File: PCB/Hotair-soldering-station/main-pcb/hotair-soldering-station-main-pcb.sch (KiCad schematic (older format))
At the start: 31 parts, among them J1 fan_reg_pot, J2 main-board-conn

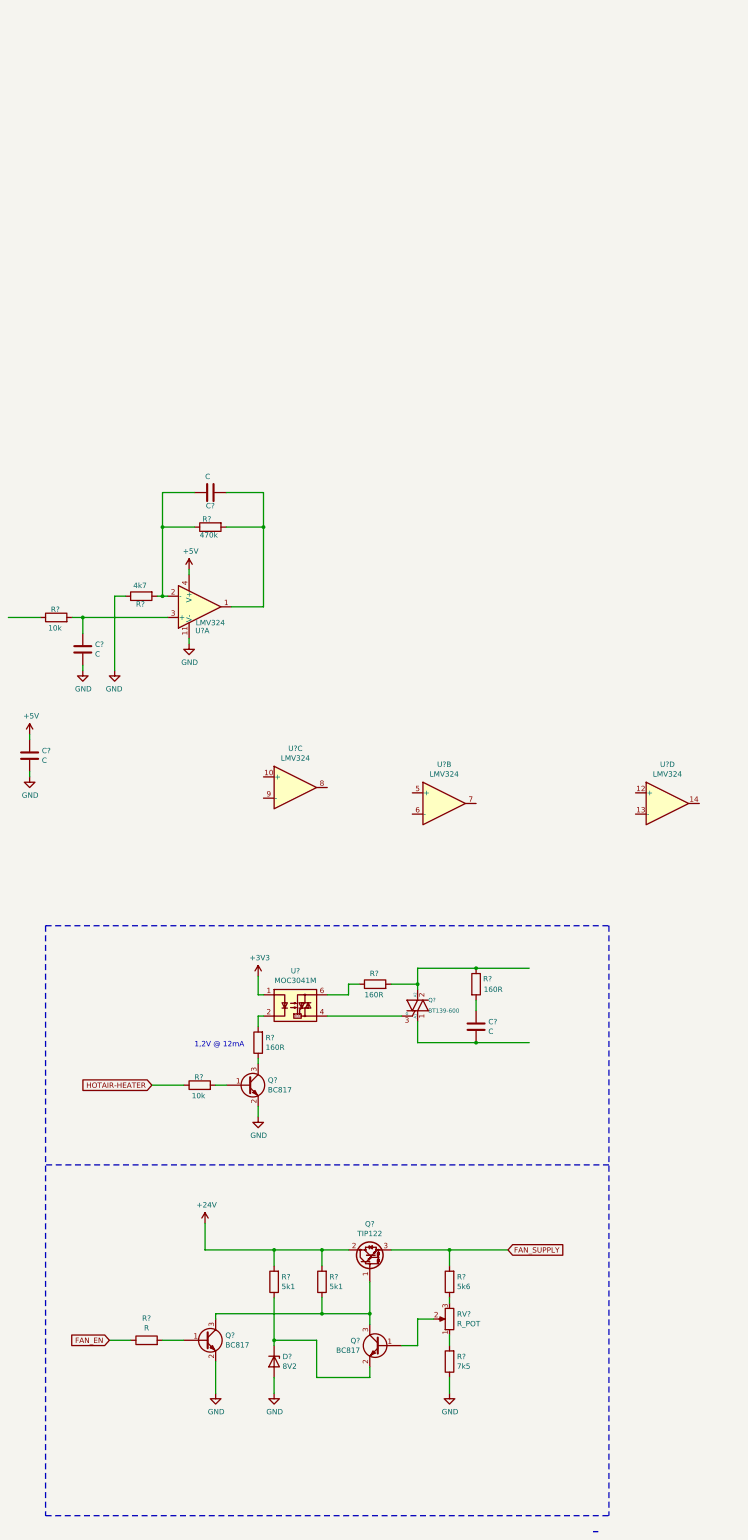
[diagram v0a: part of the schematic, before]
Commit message: schematic update
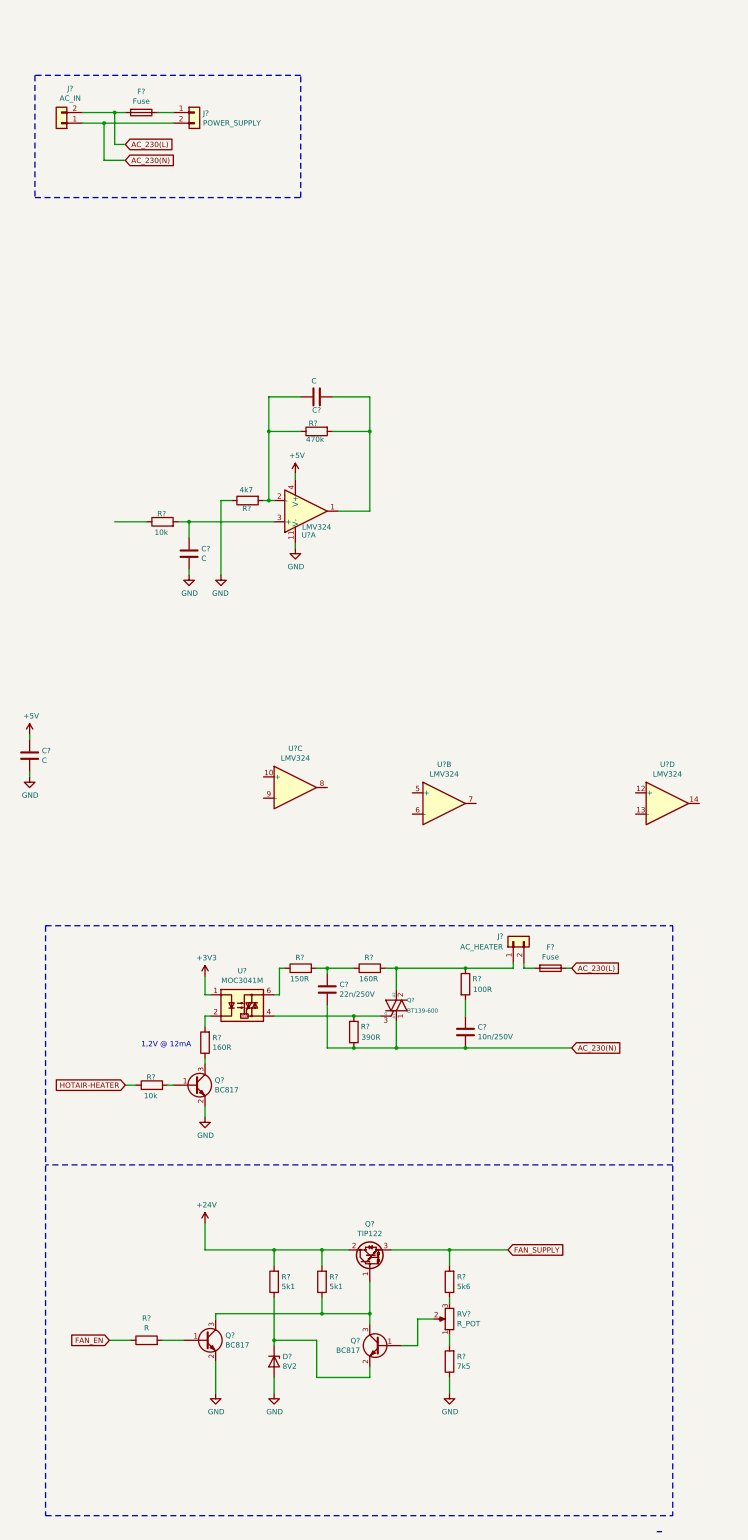
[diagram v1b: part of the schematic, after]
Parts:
- added C?: 22n/250V, symbol Device:C
- added F? (x2): Fuse, symbol Device:Fuse
- added J?: AC_HEATER, symbol Connector_Generic:Conn_01x02
- added J?: AC_IN, symbol Connector_Generic:Conn_01x02
- added J?: POWER_SUPPLY, symbol Connector_Generic:Conn_01x02
- added R?: 390R, Capacitors:0805, symbol Device:R
- added R?: 150R, Capacitors:0805, symbol Device:R
- C?: value C -> 10n/250V
- R?: value 160R -> 100R
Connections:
- net labels added: AC_230(L), AC_230(N)
- wire segments 90 -> 109
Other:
- moved on the sheet: C?, Q?, R?, U?, U?A

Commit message: add heater controll circuit, add sch block structure
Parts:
- added C?: 680u/35V, symbol Device:CP
- added D?: D_Zener, symbol Device:D_Zener
- added F?: Fuse, symbol Device:Fuse
- added J?: 24V_IN, symbol Connector_Generic:Conn_01x02
- added J?: Conn_01x05, symbol Connector_Generic:Conn_01x05
- added Q?: FP3055LP, Package_TO_SOT_THT:TO-220-3_Vertical, symbol Device:Q_NMOS_GDS
- added Q?: BC817, Package_TO_SOT_SMD:SOT-23, symbol Transistor_BJT:BC817
- added R?: 4k7, Capacitors:0805, symbol Device:R
- added R?: 1k, Capacitors:0805, symbol Device:R
- added R?: 100R, Capacitors:0805, symbol Device:R
- added R?: 4,7k, Capacitors:0805, symbol Device:R
- added R?: 10k, Capacitors:0805, symbol Device:R
- added U?: AMS1117-3.3, Package_TO_SOT_SMD:SOT-223-3_TabPin2, symbol Regulator_Linear:AMS1117-3.3
- C?: value C -> 100n
- R?: value 10k -> 1k
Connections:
- net +24V: now also C?.1, F?.1, J?.1 (Pin_1)
- net +5V: now also R?.1
- net GND: now also C?.2, D?.2 (A), J?.1 (Pin_1), J?.4 (Pin_4), J?.5 (Pin_5), Q?.2 (E), Q?.3 (S), R?.1, U?.1 (GND)
- net at C?.1, R?.2, U?.1: now also R?.1
- net SOLDERING_IRON_THERM: now reaches R?.1
- net SOLDERING_IRON_THERM: now also J?.3 (Pin_3)
- net HOTAIR-HEATER renamed HOTAIR_HEATER_CTRL
- new net: F?.2, J?.2 (Pin_2)
- new net: Q?.1 (G), R?.1
- new net: Q?.1 (B), R?.1, R?.2
- new net: Q?.3 (C), R?.2, R?.2
- new net SOLDERING_IRON_HEATER: J?.2 (Pin_2), Q?.2 (D)
- new net SOLD_IRON_HEATER_CTRL: R?.2
- new net THERM_IRON_ADC: D?.1 (K), R?.2
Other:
- note added: "Front PCB connector"
- note added: "HOT-AIR"
- note added: "Heater controll"
- note added: "SMD Rework, Soldering iron - Main PCB"
- note added: "Soldering iron"
- note added: "Soldering iron connector\n"
- note added: "Thermocouple amplifier"
- note removed: "SMD Rework, Soldering station - Front PCB"
- moved on the sheet: C?, D?, F?, J1, J2, J?, Q?, R?, RV?, U?, U?A, U?B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

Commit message: schematic update
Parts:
- added C?: 100n, symbol Device:C
- added C?: C, symbol Device:C
- added D?: D_Zener, symbol Device:D_Zener
- added J?: Conn_01x06, symbol Connector_Generic:Conn_01x06
- added J?: Conn_01x05, symbol Connector_Generic:Conn_01x05
- added R?: 470k, Capacitors:0805, symbol Device:R
- added R? (x2): 4k7, Capacitors:0805, symbol Device:R
- added R?: 1k, Capacitors:0805, symbol Device:R
- added U?: STM32F030K6Tx, Package_QFP:LQFP-32_7x7mm_P0.8mm, symbol MCU_ST_STM32F0:STM32F030K6Tx
- C?: value C -> 100n
- C?: value C -> 8,2n
- D?: value D_Zener -> 3v6
- R?: value 4k7 -> 510R
- R?: value 1k -> 39k
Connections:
- net +3V3: now also J?.2 (Pin_2), U?.1 (VDD), U?.17 (VDD), U?.5 (VDDA)
- net 7SEG_CLK: now also U?.11 (PA5)
- net 7SEG_DIN: now also U?.13 (PA7)
- net 7SEG_LATCH: now also U?.12 (PA6)
- net FAN_SUPPLY: now also J?.1 (Pin_1)
- net GND: now also C?.2, D?.2 (A), J?.3 (Pin_3), J?.4 (Pin_4), J?.5 (Pin_5), R?.1, U?.16 (VSS), U?.32 (VSS)
- net HOTAIR_DOWN_SW: now also U?.28 (PB5)
- net HOTAIR_HEATER_CTRL: now also U?.10 (PA4)
- net HOTAIR_ON_SW: now also U?.15 (PB1)
- net HOTAIR_UP_SW: now also U?.29 (PB6)
- net SOLDERING_IRON_THERM: now also J?.3 (Pin_3)
- net SOLDER_DOWN_SW: now also U?.26 (PB3)
- net SOLDER_ON_SW: now also U?.14 (PB0)
- net SOLDER_UP_SW: now also U?.27 (PB4)
- net SOLD_IRON_HEATER_CTRL: now also U?.9 (PA3)
- net THERM_IRON_ADC: now also U?.6 (PA0)
- net at U?.5 (+): now also C?.2, R?.1, R?.2
- net at U?.6 (-): now also C?.1, R?.2
- net at U?.7: now also C?.1, R?.1, R?.2
- new net BUZZER: U?.18 (PA8)
- new net HOTAIR_REED_SW: J?.2 (Pin_2), U?.30 (PB7)
- new net HOTAIR_THERM: R?.1
- new net RST: J?.1 (Pin_1), U?.4 (NRST)
- new net SWCLK: J?.5 (Pin_5), U?.24 (PA14)
- new net SWDIO: J?.4 (Pin_4), U?.23 (PA13)
- new net THERM_HOTAIR_ADC: D?.1 (K), R?.2, U?.7 (PA1)
- new net UART_DBG_TX: J?.6 (Pin_6), U?.8 (PA2)
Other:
- note added: "HOTAIR connector\n"
- moved on the sheet: C?, D?, F?, J1, J2, J?, Q?, R?, RV?, U?, U?B, U?C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

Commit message: schematic update
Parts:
- added R? (x2): 0R, Capacitors:0805, symbol Device:R
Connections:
- net GND: now also R?.1, R?.1; no longer J?.4 (Pin_4), J?.4 (Pin_4)
- new net: J?.4 (Pin_4), R?.2 (x2)
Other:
- note added: "Microcontroller"
- moved on the sheet: J?, U?
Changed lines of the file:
@@
 L Connector_Generic:Conn_01x05 J?
 U 1 1 5F810B18
-P 9525 11900
-F 0 "J?" H 9605 11942 50  0000 L CNN
-F 1 "Conn_01x05" H 9605 11851 50  0000 L CNN
-F 2 "" H 9525 11900 50  0001 C CNN
-F 3 "~" H 9525 11900 50  0001 C CNN
-	1    9525 11900
+P 9550 11900
+F 0 "J?" H 9630 11942 50  0000 L CNN
+F 1 "Conn_01x05" H 9630 11851 50  0000 L CNN
+F 2 "" H 9550 11900 50  0001 C CNN
+F 3 "~" H 9550 11900 50  0001 C CNN
+	1    9550 11900
 	1    0    0    -1
 $EndComp
@@
 L power:GND #PWR?
 U 1 1 5F812675
-P 9225 12150
-F 0 "#PWR?" H 9225 11900 50  0001 C CNN
-F 1 "GND" H 9230 11977 50  0000 C CNN
-F 2 "" H 9225 12150 50  0001 C CNN
-F 3 "" H 9225 12150 50  0001 C CNN
-	1    9225 12150
-	1    0    0    -1
-$EndComp
-Wire Wire Line
-	9175 11900 9325 11900
-Wire Wire Line
-	9325 11800 9175 11800
-Text GLabel 9175 11800 0    50   Input ~ 0
+P 9250 12150
+F 0 "#PWR?" H 9250 11900 50  0001 C CNN
+F 1 "GND" H 9255 11977 50  0000 C CNN
+F 2 "" H 9250 12150 50  0001 C CNN
+F 3 "" H 9250 12150 50  0001 C CNN
+	1    9250 12150
+	1    0    0    -1
+$EndComp
+Wire Wire Line
+	9200 11900 9350 11900
+Wire Wire Line
+	9350 11800 9200 11800
+Text GLabel 9200 11800 0    50   Input ~ 0
 SOLDERING_IRON_HEATER
-Text GLabel 9175 11900 0    50   Input ~ 0
+Text GLabel 9200 11900 0    50   Input ~ 0
 SOLDERING_IRON_THERM
 Text GLabel 10275 6575 2    50   Input ~ 0
@@
 L power:+24V #PWR?
 U 1 1 5F850C84
-P 9075 11500
-F 0 "#PWR?" H 9075 11350 50  0001 C CNN
-F 1 "+24V" H 9090 11673 50  0000 C CNN
-F 2 "" H 9075 11500 50  0001 C CNN
-F 3 "" H 9075 11500 50  0001 C CNN
-	1    9075 11500
-	1    0    0    -1
-$EndComp
-Wire Wire Line
-	9075 11700 9075 11500
-Wire Wire Line
-	9075 11700 9325 11700
-Wire Wire Line
-	9225 12000 9325 12000
-Wire Wire Line
-	9225 12000 9225 12100
+P 9100 11500
+F 0 "#PWR?" H 9100 11350 50  0001 C CNN
+F 1 "+24V" H 9115 11673 50  0000 C CNN
+F 2 "" H 9100 11500 50  0001 C CNN
+F 3 "" H 9100 11500 50  0001 C CNN
+	1    9100 11500
+	1    0    0    -1
+$EndComp
+Wire Wire Line
+	9100 11700 9100 11500
+Wire Wire Line
+	9100 11700 9350 11700
 $Comp
 L power:+24V #PWR?
@@
 L Regulator_Linear:AMS1117-3.3 U?
 U 1 1 5F87AB31
-P 5375 2450
-F 0 "U?" H 5375 2692 50  0000 C CNN
-F 1 "AMS1117-3.3" H 5375 2601 50  0000 C CNN
-F 2 "Package_TO_SOT_SMD:SOT-223-3_TabPin2" H 5375 2650 50  0001 C CNN
-F 3 "http://www.advanced-monolithic.com/pdf/ds1117.pdf" H 5475 2200 50  0001 C CNN
-	1    5375 2450
+P 6025 2350
+F 0 "U?" H 6025 2592 50  0000 C CNN
+F 1 "AMS1117-3.3" H 6025 2501 50  0000 C CNN
+F 2 "Package_TO_SOT_SMD:SOT-223-3_TabPin2" H 6025 2550 50  0001 C CNN
+F 3 "http://www.advanced-monolithic.com/pdf/ds1117.pdf" H 6125 2100 50  0001 C CNN
+	1    6025 2350
 	1    0    0    -1
 $EndComp
@@
 L power:GND #PWR?
 U 1 1 5F9705C8
-P 5375 2800
-F 0 "#PWR?" H 5375 2550 50  0001 C CNN
-F 1 "GND" H 5380 2627 50  0000 C CNN
-F 2 "" H 5375 2800 50  0001 C CNN
-F 3 "" H 5375 2800 50  0001 C CNN
-	1    5375 2800
-	1    0    0    -1
-$EndComp
-Wire Wire Line
-	5375 2800 5375 2750
+P 6025 2700
+F 0 "#PWR?" H 6025 2450 50  0001 C CNN
+F 1 "GND" H 6030 2527 50  0000 C CNN
+F 2 "" H 6025 2700 50  0001 C CNN
+F 3 "" H 6025 2700 50  0001 C CNN
+	1    6025 2700
+	1    0    0    -1
+$EndComp
+Wire Wire Line
+	6025 2700 6025 2650
 $Comp
 L Device:R R?
@@
 SOLDERING_IRON_THERM
 Wire Wire Line
-	9325 12100 9225 12100
-Connection ~ 9225 12100
-Wire Wire Line
-	9225 12100 9225 12150
+	9350 12100 9250 12100
+Wire Wire Line
+	9250 12100 9250 12150
 Wire Notes Line
 	7325 10875 11775 10875
@@
 	4425 11825 4725 11825
 Connection ~ 4425 11825
-Text GLabel 2100 11925 0    50   Input ~ 0
-HOTAIR_THERM
 Text GLabel 4725 11825 2    50   Input ~ 0
 THERM_HOTAIR_ADC
@@
 L Connector_Generic:Conn_01x05 J?
 U 1 1 5FAE215C
-P 2925 13900
-F 0 "J?" H 3005 13942 50  0000 L CNN
-F 1 "Conn_01x05" H 3005 13851 50  0000 L CNN
-F 2 "" H 2925 13900 50  0001 C CNN
-F 3 "~" H 2925 13900 50  0001 C CNN
-	1    2925 13900
+P 2900 13900
+F 0 "J?" H 2980 13942 50  0000 L CNN
+F 1 "Conn_01x05" H 2980 13851 50  0000 L CNN
+F 2 "" H 2900 13900 50  0001 C CNN
+F 3 "~" H 2900 13900 50  0001 C CNN
+	1    2900 13900
 	1    0    0    -1
 $EndComp
@@
 L power:GND #PWR?
 U 1 1 5FAE2162
-P 2625 14150
-F 0 "#PWR?" H 2625 13900 50  0001 C CNN
-F 1 "GND" H 2630 13977 50  0000 C CNN
-F 2 "" H 2625 14150 50  0001 C CNN
-F 3 "" H 2625 14150 50  0001 C CNN
-	1    2625 14150
-	1    0    0    -1
-$EndComp
-Wire Wire Line
-	2575 13900 2725 13900
-Wire Wire Line
-	2725 13800 2575 13800
-Text GLabel 2575 13900 0    50   Input ~ 0
+P 2600 14150
+F 0 "#PWR?" H 2600 13900 50  0001 C CNN
+F 1 "GND" H 2605 13977 50  0000 C CNN
+F 2 "" H 2600 14150 50  0001 C CNN
+F 3 "" H 2600 14150 50  0001 C CNN
+	1    2600 14150
+	1    0    0    -1
+$EndComp
+Wire Wire Line
+	2550 13900 2700 13900
+Wire Wire Line
+	2700 13800 2550 13800
+Text GLabel 2550 13900 0    50   Input ~ 0
 SOLDERING_IRON_THERM
-Wire Wire Line
-	2625 14000 2725 14000
-Wire Wire Line
-	2625 14000 2625 14100
-Wire Wire Line
-	2725 14100 2625 14100
-Connection ~ 2625 14100
-Wire Wire Line
-	2625 14100 2625 14150
 Text Notes 775  13075 0    98   ~ 0
 HOTAIR connector\n
@@
 Wire Notes Line
 	650  4925 650  14675
-Text GLabel 2575 13800 0    50   Input ~ 0
+Text GLabel 2550 13800 0    50   Input ~ 0
 HOTAIR_REED_SW
-Text GLabel 2575 13700 0    50   Input ~ 0
+Text GLabel 2550 13700 0    50   Input ~ 0
 FAN_SUPPLY
 Wire Wire Line
-	2575 13700 2725 13700
+	2550 13700 2700 13700
 Wire Notes Line
 	6950 5550 12675 5550
+Text Notes 12950 5450 0    236  ~ 47
+Microcontroller
+Text GLabel 2100 11925 0    50   Input ~ 0
+HOTAIR_THERM
+$Comp
+L Device:R R?
+U 1 1 5F8115BA
+P 2450 14000
+F 0 "R?" V 2275 14050 50  0000 R CNN
+F 1 "0R" V 2350 14050 50  0000 R CNN
+F 2 "Capacitors:0805" V 2380 14000 50  0001 C CNN
+F 3 "~" H 2450 14000 50  0001 C CNN
+	1    2450 14000
+	0    -1   -1   0
+$EndComp
+Wire Wire Line
+	2700 14100 2600 14100
+Wire Wire Line
+	2600 14100 2600 14150
+Wire Wire Line
+	2700 14000 2600 14000
+$Comp
+L power:GND #PWR?
+U 1 1 5F839D58
+P 2300 14150
+F 0 "#PWR?" H 2300 13900 50  0001 C CNN
+F 1 "GND" H 2305 13977 50  0000 C CNN
+F 2 "" H 2300 14150 50  0001 C CNN
+F 3 "" H 2300 14150 50  0001 C CNN
+	1    2300 14150
+	1    0    0    -1
+$EndComp
+Wire Wire Line
+	2300 14150 2300 14000
+$Comp
+L Device:R R?
+U 1 1 5F8479CC
+P 9100 12000
+F 0 "R?" V 9000 12050 50  0000 R CNN
+F 1 "0R" V 8925 12050 50  0000 R CNN
+F 2 "Capacitors:0805" V 9030 12000 50  0001 C CNN
+F 3 "~" H 9100 12000 50  0001 C CNN
+	1    9100 12000
+	0    -1   -1   0
+$EndComp
+Wire Wire Line
+	9350 12000 9250 12000
+$Comp
+L power:GND #PWR?
+U 1 1 5F864043
+P 8900 12150
+F 0 "#PWR?" H 8900 11900 50  0001 C CNN
+F 1 "GND" H 8905 11977 50  0000 C CNN
+F 2 "" H 8900 12150 50  0001 C CNN
+F 3 "" H 8900 12150 50  0001 C CNN
+	1    8900 12150
+	1    0    0    -1
+$EndComp
+Wire Wire Line
+	8900 12150 8900 12000
+Wire Wire Line
+	8900 12000 8950 12000
 $EndSCHEMATC

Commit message: main schematic update, front pcb routing
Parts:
- added C? (x3): 100n, symbol Device:C
- added C?: 47u, symbol Device:CP
- added C?: 10u, symbol Device:CP
- added MOD?: LM2596-Step-Down, symbol My-Lib:LM2596-Step-Down
- added R?: 0R, Capacitors:0805, symbol Device:R
- added R?: 4k7, Capacitors:0805, symbol Device:R
- added R? (x4): 10k, Capacitors:0805, symbol Device:R
- added U?: DS18B20, Package_TO_SOT_THT:TO-92_Inline, symbol Sensor_Temperature:DS18B20
- C?: value C -> 8n2
- J?: value Conn_01x05 -> SOLD_IRON_CONN
- J?: value Conn_01x06 -> ICP
- J?: value Conn_01x05 -> HOTAIR
- R?: value 4k7 -> 510R
- RV?: value R_POT -> 10k
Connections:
- net +24V: now also MOD?.2 (IN+)
- net +3V3: now also U?.2 (VO), C?.1, C?.1, C?.1, C?.1, R?.1, U?.3 (VDD)
- net +5V: now also U?.3 (VI), C?.1, MOD?.4 (OUT+)
- net FAN_EN: now also U?.20 (PA10)
- net GND: now also C?.2, C?.2, C?.2, C?.2, C?.2, MOD?.1 (IN-), MOD?.3 (OUT-), R?.1, R?.1, R?.2, U?.1 (GND); no longer Q?.3 (S)
- net at C?.2, R?.1, R?.2: now also U?.9 (-); no longer U?.5 (+)
- net at C?.1, R?.2: now also U?.5 (+), U?.8; no longer R?.1, U?.7
- net at C?.1, R?.2: now also U?.10 (+); no longer U?.6 (-)
- net at C?.1, R?.2, U?.1: now also U?.12 (+); no longer R?.1
- net at U?.13 (-): now also R?.1, R?.2
- net at U?.14: now also R?.1, R?.2
- net at U?.19 (PA9): now also R?.2, U?.2 (DQ)
- new net: R?.1, R?.2, U?.7
- new net: Q?.3 (S), R?.1
- new net: R?.1, R?.2, U?.6 (-)
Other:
- note added: "Fan speed controll"
- note added: "Supply connectors, voltage regulation"
- moved on the sheet: C?, D?, F?, J?, Q?, R?, RV?, U?, U?A, U?B, U?C, U?D

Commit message: Draw main PCB digital schematic parts, add footprints, connectors unification
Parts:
- removed J1: fan_reg_pot, Connector_PinHeader_2.54mm:PinHeader_1x03_P2.54mm_Vertical, symbol Connector_Generic:Conn_01x03
- removed J?: 24V_IN, symbol Connector_Generic:Conn_01x02
- removed J?: AC_IN, symbol Connector_Generic:Conn_01x02
- removed J?: HOTAIR, symbol Connector_Generic:Conn_01x05
- removed MOD?: LM2596-Step-Down, symbol My-Lib:LM2596-Step-Down
- removed RV?: 10k, symbol Device:R_POT
- added C?: 330u/35V, Capacitors_THT:CP_Radial_D10.0mm_P5.00mm, symbol Device:CP
- added D?: 3v6, Diode_THT:D_DO-41_SOD81_P10.16mm_Horizontal, symbol Device:D_Zener
- added J?: HOTAIR_FAN, Connectors_JST:JST_XH_B02B-XH-A_02x2.50mm_Straight, symbol Connector_Generic:Conn_01x02
- added J?: HOTAIR_MEAS, Connectors_JST:JST_XH_B03B-XH-A_03x2.50mm_Straight, symbol Connector_Generic:Conn_01x03
- added J?: 24V_IN, symbol Connector_Generic:Conn_01x04
- added J?: EARTH_GND, symbol Connector:Screw_Terminal_01x02
- added J?: 230VAC_IN, symbol Connector:Screw_Terminal_01x03
- added LS?: BUZZER, My-Footprints:Buzzer, symbol SparkFun-Electromechanical:BUZZER-PTH
- added Q?: BC817, Package_TO_SOT_SMD:SOT-23, symbol Transistor_BJT:BC817
- added R?: 10k, Capacitors:0805, symbol Device:R
- added U?: MP1584-Step-Down, My-Footprints:MP1584_Mini_3A_Step_Down_Conv, symbol My-Lib:MP1584-Step-Down
- C?: footprint (none) -> Capacitors_THT:C_Rect_L18.0mm_W5.0mm_P15.00mm_FKS3_FKP3
- C? (x8): footprint (none) -> Capacitors:0805
- C?: value 680u/35V -> 330u/35V; footprint (none) -> Capacitors_THT:CP_Radial_D10.0mm_P5.00mm
- C?: value 47u -> 100u/10V; footprint (none) -> Capacitors_THT:CP_Radial_D5.0mm_P2.00mm
- C?: value 10u -> 47u/10V; footprint (none) -> Capacitors_THT:CP_Radial_D5.0mm_P2.00mm
- D?: value D_Zener -> 3V6; footprint (none) -> Diodes_SMD:D_MiniMELF
- D?: footprint (none) -> Diodes_SMD:D_MiniMELF
- J2: footprint My-Footprints:Con-01x14 -> My-Footprints:Conn-01x14
- J?: value AC_HEATER -> HOTAIR_HEATER; footprint (none) -> Connectors_Hirose:Hirose_DF63-2P-3.96DSA_02x3.96mm_Straight
- J?: footprint (none) -> My-Footprints:Conn-01x05-N25-W5P
- J?: footprint (none) -> My-Footprints:Conn-01x06
- Q?: value TIP122 -> BD681; footprint Package_TO_SOT_THT:TO-220-3_Vertical -> TO_SOT_Packages_THT:TO-126_Vertical
- R?: value R -> 10k; footprint (none) -> Capacitors:0805
- R?: value 1k -> 39k
- U?: footprint (none) -> Housings_DIP:DIP-6_W7.62mm_LongPads
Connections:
- net +24V: now also C?.1, U?.1 (IN+)
- net +3V3: now also D?.1 (K)
- net +5V: now also LS?.- (2), U?.4 (OUT+)
- net AC_230(L): now also J?.3 (Pin_3)
- net AC_230(N): now also J?.2 (Pin_2)
- net BUZZER: now also R?.2
- net FAN_SUPPLY: now also J?.1 (Pin_1)
- net GND: now also C?.2, D?.2 (A), J?.1 (Pin_1), J?.2 (Pin_2), J?.2 (Pin_2), Q?.2 (E), U?.2 (IN-), U?.3 (OUT-)
- net HOTAIR_REED_SW: now also J?.3 (Pin_3)
- net SOLDERING_IRON_THERM: now also J?.1 (Pin_1)
- net FAN_POT_W: now reaches Q?.1 (B)
- net FAN_POT_W: now also J2.7 (Pin_7)
- net FAN_POT_B: now reaches R?.1
- net FAN_POT_B: now also J2.6 (Pin_6)
- net FAN_POT_A: now reaches R?.2
- net FAN_POT_A: now also J2.5 (Pin_5)
- net at F?.2: now also J?.3 (Pin_3), J?.4 (Pin_4)
- net at R?.2: now also J?.2 (Pin_2)
- new net: J?.1 (Pin_1), J?.1 (Pin_1), J?.2 (Pin_2)
- new net: LS?.+ (1), Q?.3 (C)
- new net: Q?.1 (B), R?.1
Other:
- moved on the sheet: C?, D?, F?, J2, R?
